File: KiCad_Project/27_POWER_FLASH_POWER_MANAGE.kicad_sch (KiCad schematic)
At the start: 16 parts, among them U4 SY8089AAAC

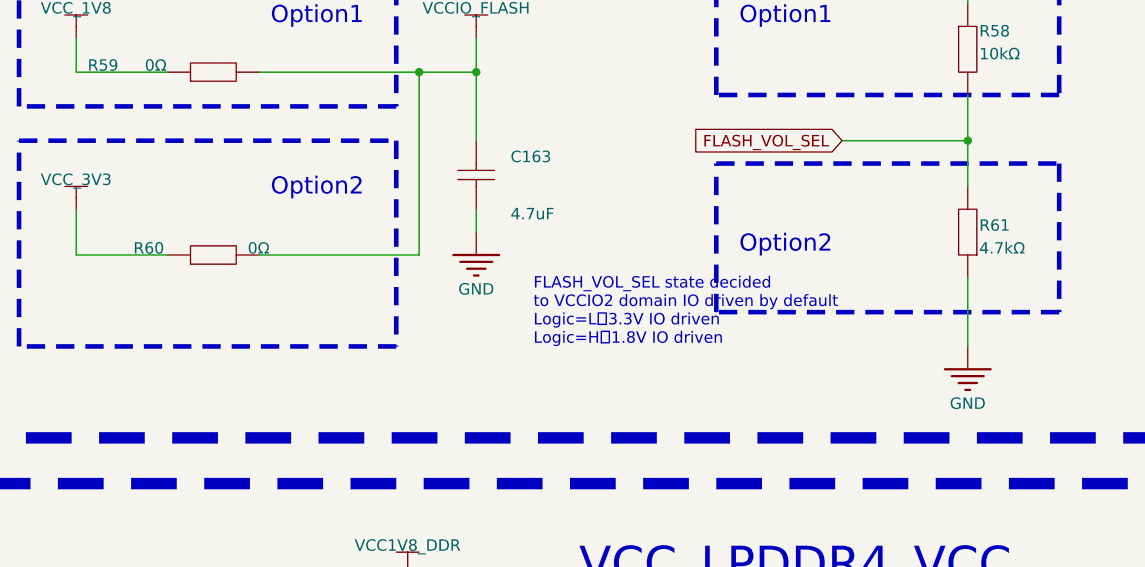
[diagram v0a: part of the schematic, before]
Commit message: Update additional PCBs
Add WIFI PCB to get best antenna
Add Display Debbugger to get interface pinout
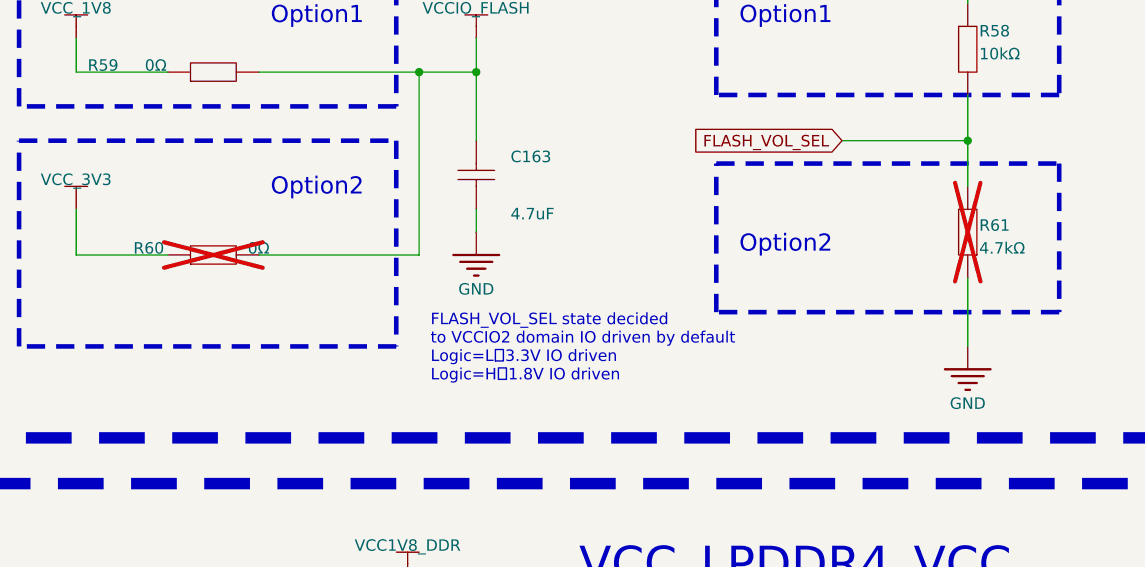
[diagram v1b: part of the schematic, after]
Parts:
- R60, R61: now not fitted; now left out of the parts list
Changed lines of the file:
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@@
 	(text "FLASH_VOL_SEL state decided \nto VCCIO2 domain IO driven by default\nLogic=L：3.3V IO driven\nLogic=H：1.8V IO driven"
 		(exclude_from_sim no)
-		(at 189.23 101.6 0)
+		(at 177.8 105.664 0)
 		(effects
 			(font
@@
 		(unit 1)
 		(exclude_from_sim no)
-		(in_bom yes)
+		(in_bom no)
 		(on_board yes)
-		(dnp no)
+		(dnp yes)
 		(property "Reference" "R60"
 			(at 144.78 91.44 0)
@@
 		(unit 1)
 		(exclude_from_sim no)
-		(in_bom yes)
+		(in_bom no)
 		(on_board yes)
-		(dnp no)
+		(dnp yes)
 		(property "Reference" "R61"
 			(at 238.76 88.9 90)
